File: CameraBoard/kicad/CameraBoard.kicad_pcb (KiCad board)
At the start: 2 copper layers, 101.6 x 76.2 mm, 100 parts, among them Q1 SI7465DP-T1-E3, Q2 BVSS123LT1G, Q3 BSS84, U1 MP26124GR-Z, U2 TPS63070, U3 LM2678SD-12/NOPB, U4 TS5A3159ADBVR, U5 ICM7242IBAZ-SMD, U6 H11F1SR2M, U7 H11F1SR2M, U8 SN74LVC1G17DCKR

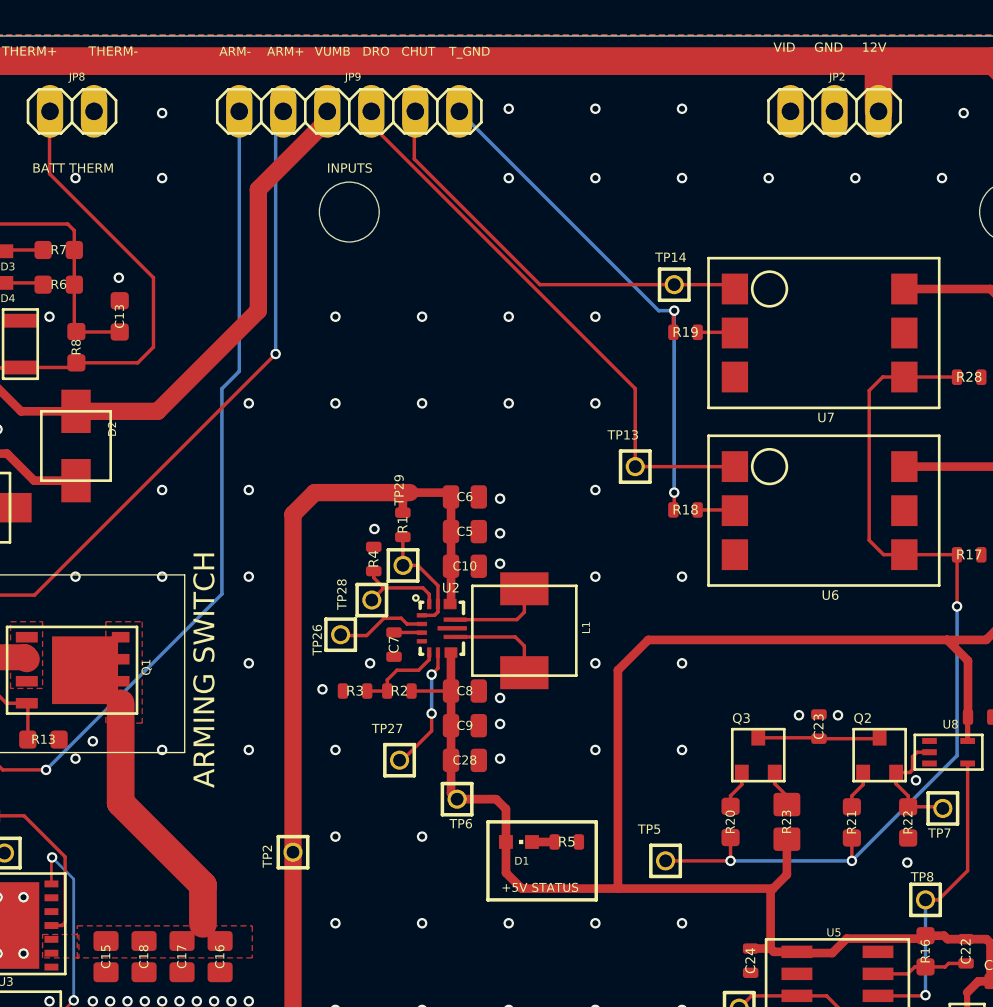
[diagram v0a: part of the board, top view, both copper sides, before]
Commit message: Updated KiCAD EAGLE import to latest KiCAD 9.0.2.
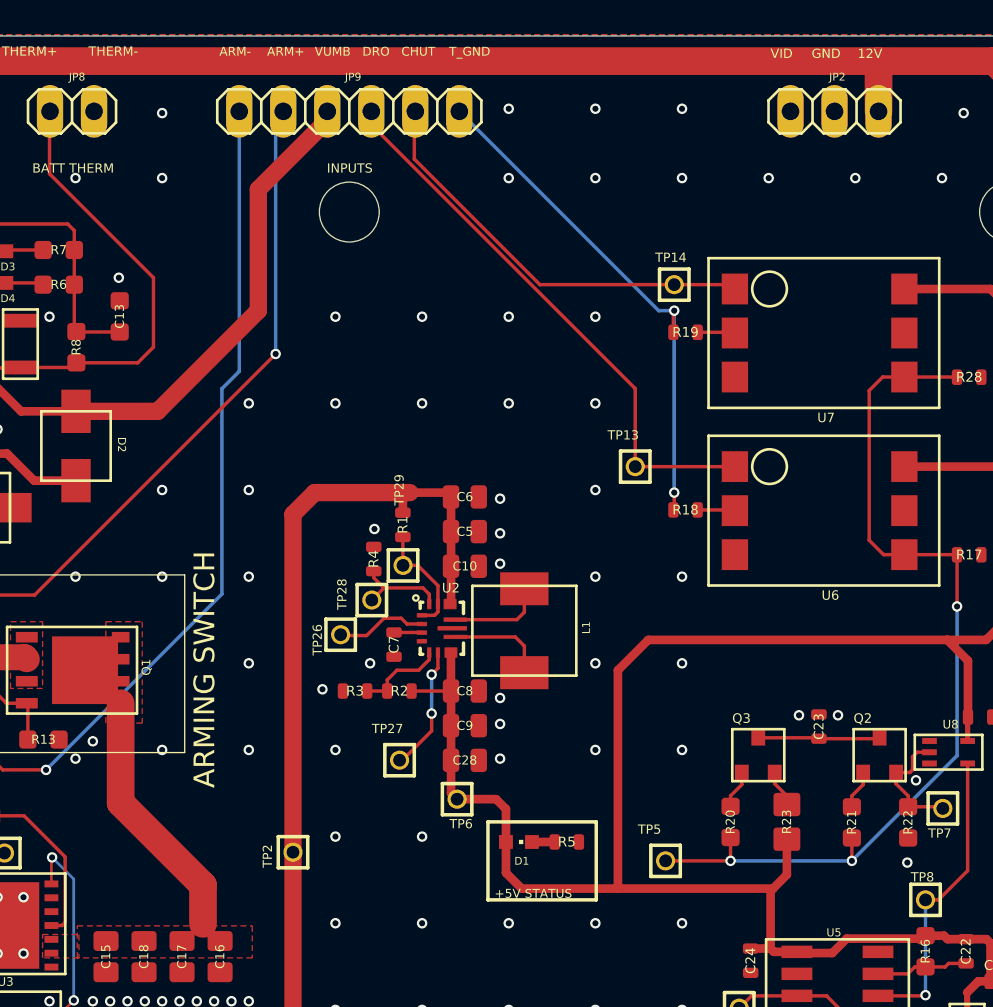
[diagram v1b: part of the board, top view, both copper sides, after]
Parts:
- D1, D3, D4: footprint CameraBoard:CHIPLED_0603 -> CameraBoard:CHIPLED_0603_259
- JP1, JP10, JP12, JP13, JP2, JP3, JP4, JP5, JP6, JP7: value (none) -> PINHD-1X3; footprint CameraBoard:1X03 -> CameraBoard:1X03_325
- JP11, JP9: value (none) -> PINHD-1X6; footprint CameraBoard:1X06 -> CameraBoard:1X06_325
- JP8: value (none) -> PINHD-1X2; footprint CameraBoard:1X02 -> CameraBoard:1X02_325
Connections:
- net ARM-IN renamed /CameraBoard_1/ARM-IN
- net ARM-OUT renamed /CameraBoard_1/ARM-OUT
- net BATT+ renamed /CameraBoard_1/BATT+
- net CAM_DOWN renamed /CameraBoard_2/CAM_DOWN
- net CAM_UP renamed /CameraBoard_2/CAM_UP
- net SCHMITTIN renamed Net-(Q2-S)
- net SOUT renamed /CameraBoard_1/SOUT
- net TIMERPULSE renamed /CameraBoard_2/TIMERPULSE
- net TIMER_TRIGG renamed /CameraBoard_2/TIMER_TRIGG
- net TPS-EN renamed Net-(U2-EN)
- net TPS-FB renamed Net-(U2-FB)
- net TPS-FB2 renamed Net-(U2-FB2)
- net TPS-L1 renamed Net-(U2-L1)
- net TPS-L2 renamed Net-(U2-L2)
- net TPS-PG renamed Net-(U2-PG)
- net TPS-VAUX renamed Net-(U2-VAUX)
- net TPS-VSEL renamed Net-(U2-VSEL)
- net VUMB renamed /CameraBoard_1/VUMB
- net ~{TIMER_OUTPUT} renamed /CameraBoard_2/~{TIMER_OUTPUT}
- JP1 pad 3: (no net) -> unconnected-(JP1-Pad3)
- JP2 pad 3: (no net) -> unconnected-(JP2-Pad3)
- JP3 pad 3: (no net) -> unconnected-(JP3-Pad3)
- JP4 pad 3: (no net) -> unconnected-(JP4-Pad3)
- JP5 pad 3: (no net) -> unconnected-(JP5-Pad3)
- JP6 pad 3: (no net) -> unconnected-(JP6-Pad3)
- JP7 pad 3: (no net) -> unconnected-(JP7-Pad3)
- U5 pad 1: (no net) -> unconnected-(U5-/2-Pad1)
- U5 pad 7: (no net) -> unconnected-(U5-TB-Pad7)
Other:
- board text added: "12V SPS"
- board text added: "5V SPS"
- board text added: "Inputs"
- board text added: "LiPo Charger"
- board text added: "Pulse Generator"
- board text added: "Timer"

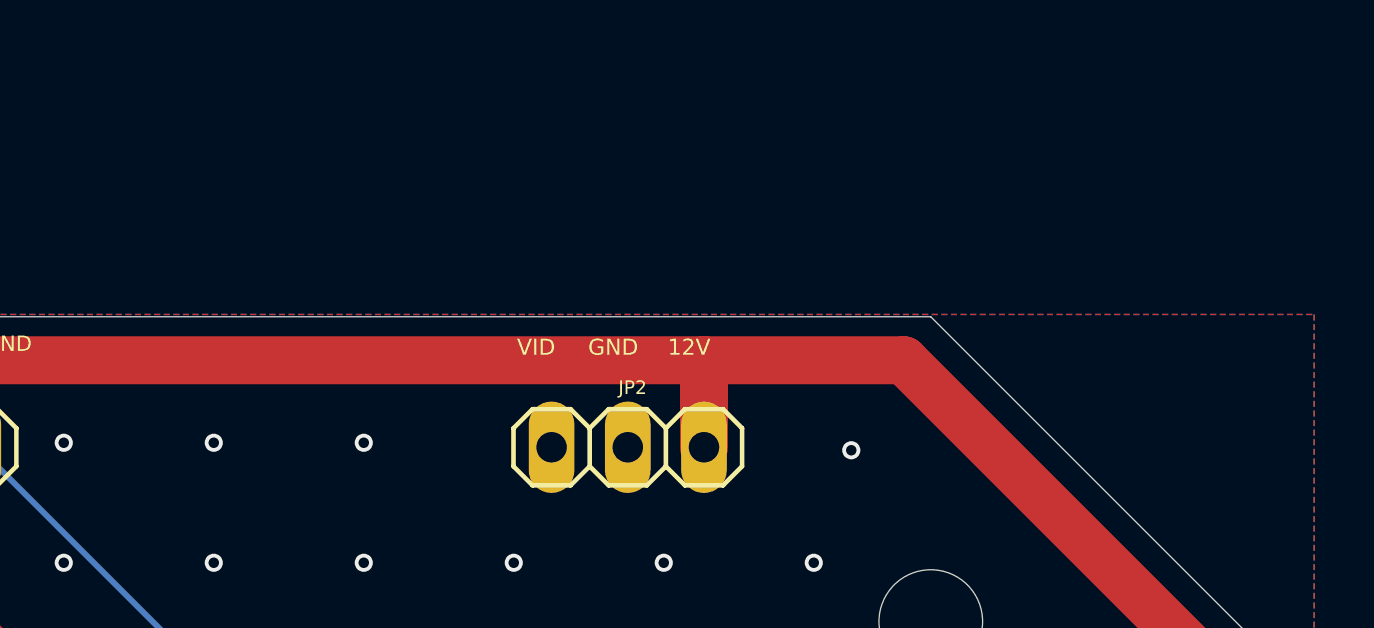
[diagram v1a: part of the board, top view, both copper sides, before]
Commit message: Changed pulldown to 150k and added note about flipped connector.
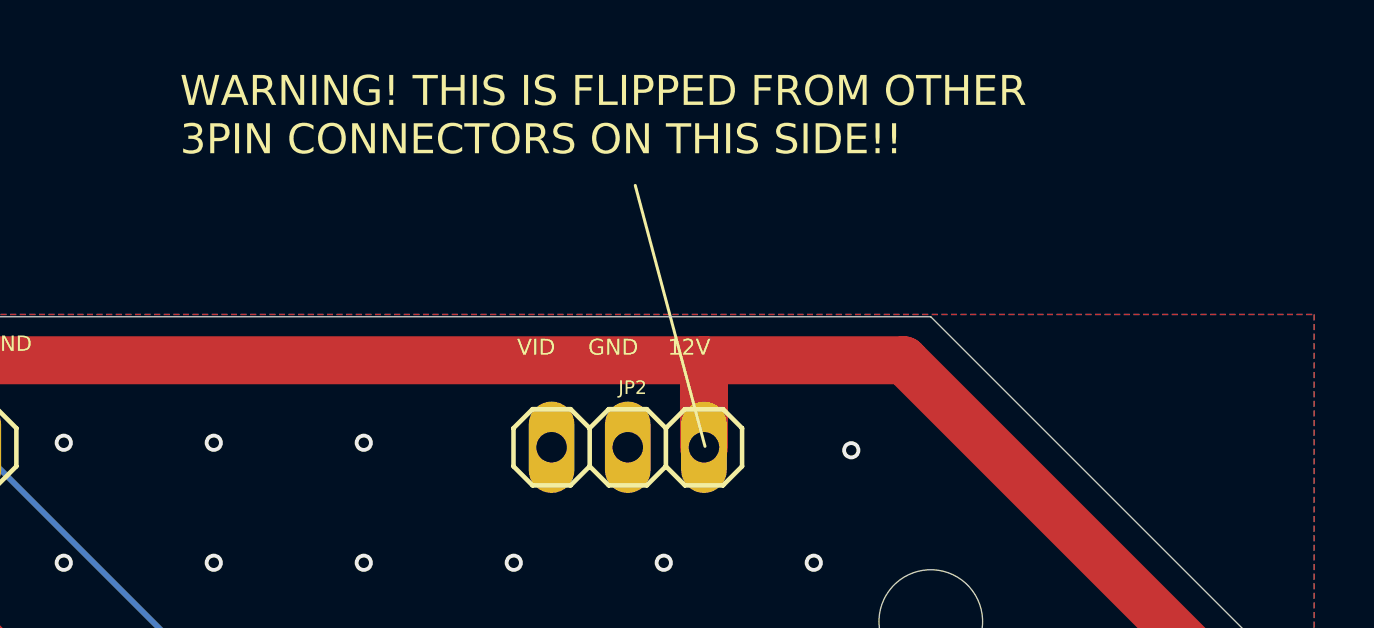
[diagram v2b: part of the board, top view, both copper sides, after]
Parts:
- R13: value 10k -> 150k
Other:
- board text added: "WARNING! THIS IS FLIPPED FROM OTHER 3PIN CONNECTORS ON THIS SIDE!!"
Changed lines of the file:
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@@
 			)
 		)
-		(property "Datasheet" ""
+		(property "Datasheet" "https://www.monolithicpower.com/en/documentview/productdocument/index/version/2/document_type/Datasheet/lang/en/sku/MP26124/document_id/3740"
 			(at 0 0 180)
 			(layer "F.Fab")
@@
 			)
 		)
-		(property "Value" "10k"
+		(property "Value" "150k"
 			(at -1.4 1.75 0)
 			(unlocked yes)
@@
 	)
 	(gr_line
+		(start 176.75 62.525)
+		(end 179.075 71.225)
+		(stroke
+			(width 0.1)
+			(type default)
+		)
+		(layer "F.SilkS")
+	)
+	(gr_line
 		(start 156.5011 116.7536)
 		(end 162.7511 116.7536)
@@
 			)
 			(justify left bottom)
+		)
+	)
+	(gr_text "WARNING! THIS IS FLIPPED FROM OTHER \n3PIN CONNECTORS ON THIS SIDE!!"
+		(at 161.575 61.575 0)
+		(layer "F.SilkS")
+		(effects
+			(font
+				(size 1 1)
+				(thickness 0.1)
+			)
+			(justify left bottom)

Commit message: Cleaned up second page - fixed optoisolator symbols, added notes about levels and times, and cleaned up alot. Put in notes about mod wires.
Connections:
- net VIDEO_OUT renamed Net-(U4-COM)
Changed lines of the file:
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@@
 	(net 37 "/CameraBoard_2/CAM_DOWN")
 	(net 38 "/CameraBoard_2/CAM_UP")
-	(net 39 "VIDEO_OUT")
+	(net 39 "Net-(U4-COM)")
 	(net 40 "Net-(U2-L1)")
 	(net 41 "Net-(U2-L2)")
@@
 			(net 24 "unconnected-(JP2-Pad3)")
 			(pinfunction "3")
-			(pintype "passive")
+			(pintype "passive+no_connect")
 			(solder_mask_margin 0.0635)
 			(thermal_bridge_angle 0)
@@
 			(layers "*.Cu" "*.Mask")
 			(remove_unused_layers no)
-			(net 39 "VIDEO_OUT")
+			(net 39 "Net-(U4-COM)")
 			(pinfunction "1")
 			(pintype "passive")
@@
 			(net 30 "DROGUE")
 			(pinfunction "ANOD")
-			(pintype "bidirectional")
+			(pintype "passive")
 			(solder_mask_margin 0.0635)
 			(solder_paste_margin 0)
@@
 			(net 54 "Net-(U6-CAT)")
 			(pinfunction "CAT")
-			(pintype "bidirectional")
+			(pintype "passive")
 			(solder_mask_margin 0.0635)
 			(solder_paste_margin 0)
@@
 			(net 11 "+5V")
 			(pinfunction "IN")
-			(pintype "bidirectional")
+			(pintype "passive")
 			(solder_mask_margin 0.0635)
 			(solder_paste_margin 0)
@@
 			(net 53 "/CameraBoard_2/TIMERPULSE")
 			(pinfunction "OUT")
-			(pintype "bidirectional")
+			(pintype "passive")
 			(solder_mask_margin 0.0635)
 			(solder_paste_margin 0)
@@
 			(net 26 "unconnected-(JP4-Pad3)")
 			(pinfunction "3")
-			(pintype "passive")
+			(pintype "passive+no_connect")
 			(solder_mask_margin 0.0635)
 			(thermal_bridge_angle 0)
@@
 			(net 28 "unconnected-(JP6-Pad3)")
 			(pinfunction "3")
-			(pintype "passive")
+			(pintype "passive+no_connect")
 			(solder_mask_margin 0.0635)
 			(thermal_bridge_angle 0)
@@
 			(net 25 "unconnected-(JP3-Pad3)")
 			(pinfunction "3")
-			(pintype "passive")
+			(pintype "passive+no_connect")
 			(solder_mask_margin 0.0635)
 			(thermal_bridge_angle 0)
@@
 			(net 32 "CHUTE")
 			(pinfunction "ANOD")
-			(pintype "bidirectional")
+			(pintype "passive")
 			(solder_mask_margin 0.0635)
 			(solder_paste_margin 0)
@@
 			(net 55 "Net-(U7-CAT)")
 			(pinfunction "CAT")
-			(pintype "bidirectional")
+			(pintype "passive")
 			(solder_mask_margin 0.0635)
 			(solder_paste_margin 0)
@@
 			(net 11 "+5V")
 			(pinfunction "IN")
-			(pintype "bidirectional")
+			(pintype "passive")
 			(solder_mask_margin 0.0635)
 			(solder_paste_margin 0)
@@
 			(net 53 "/CameraBoard_2/TIMERPULSE")
 			(pinfunction "OUT")
-			(pintype "bidirectional")
+			(pintype "passive")
 			(solder_mask_margin 0.0635)
 			(solder_paste_margin 0)
@@
 			(net 23 "unconnected-(JP1-Pad3)")
 			(pinfunction "3")
-			(pintype "passive")
+			(pintype "passive+no_connect")
 			(solder_mask_margin 0.0635)
 			(thermal_bridge_angle 0)
@@
 			)
 		)
-		(property "Datasheet" ""
+		(property "Datasheet" "https://www.renesas.com/en/document/dst/icm7242-datasheet"
 			(at 0 0 270)
 			(layer "F.Fab")
@@
 			(net 61 "unconnected-(U5-{slash}2-Pad1)")
 			(pinfunction "/2")
-			(pintype "bidirectional")
+			(pintype "bidirectional+no_connect")
 			(solder_mask_margin 0.0635)
 			(solder_paste_margin 0)
@@
 			(net 62 "unconnected-(U5-TB-Pad7)")
 			(pinfunction "TB")
-			(pintype "bidirectional")
+			(pintype "bidirectional+no_connect")
 			(solder_mask_margin 0.0635)
 			(solder_paste_margin 0)
@@
 			(net 29 "unconnected-(JP7-Pad3)")
 			(pinfunction "3")
-			(pintype "passive")
+			(pintype "passive+no_connect")
 			(solder_mask_margin 0.0635)
 			(thermal_bridge_angle 0)
@@
 			)
 		)
-		(sheetname "/CameraBoard_1/")
-		(sheetfile "CameraBoard_1.kicad_sch")
+		(sheetname "/CameraBoard_2/")
+		(sheetfile "CameraBoard_2.kicad_sch")
 		(fp_line
 			(start -1.905 1.27)
@@
 			(layers "*.Cu" "*.Mask")
 			(remove_unused_layers no)
-			(net 39 "VIDEO_OUT")
+			(net 39 "Net-(U4-COM)")
 			(pinfunction "3")
 			(pintype "passive")
@@
 			(size 0.35 0.85)
 			(layers "F.Cu" "F.Mask" "F.Paste")
-			(net 39 "VIDEO_OUT")
+			(net 39 "Net-(U4-COM)")
 			(pinfunction "COM")
 			(pintype "bidirectional")
@@
 			(net 27 "unconnected-(JP5-Pad3)")
 			(pinfunction "3")
-			(pintype "passive")
+			(pintype "passive+no_connect")
 			(solder_mask_margin 0.0635)
 			(thermal_bridge_angle 0)

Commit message: Minor updates to PCB
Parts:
- D1: value SML-D12U1WT86 -> GRN
- turned JP2 to 0 degrees
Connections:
- JP10 pad 1: +5V -> +12V
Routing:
- net +5V: track 141.7 -> 134.4 mm
- net +12V: track 425.4 -> 428.4 mm
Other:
- board text removed: "WARNING! THIS IS FLIPPED FROM OTHER 3PIN CONNECTORS ON THIS SIDE!!"
